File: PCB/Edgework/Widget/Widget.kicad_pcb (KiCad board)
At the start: 4 copper layers, 61 x 30 mm, 82 parts, among them J1 Edgework, J10 4, J11 SDA, J12 SCL, J13 1, J14 0, J15 5V, J16 3V3, J17 GND, J18 5V, J19 3V3, J2 ICSP, J20 GND, J21 5V, J22 3V3, J23 GND, J24 5V, J25 3V3, J26 GND, J3 11, J4 10, J5 9, J6 8, J7 7, J8 6, J9 5, Q1 Q_PMOS_GSD, Q2 Q_NMOS_GSD, Q3 Q_PMOS_GSD, Q4 Q_NMOS_GSD, Q5 Q_PMOS_GSD, Q6 Q_NMOS_GSD, Q7 Q_PMOS_GSD, Q8 Q_NMOS_GSD, U1 THVD1420DRLR, U2 PIC18F15Q40, U4 CM1293A‐04SO

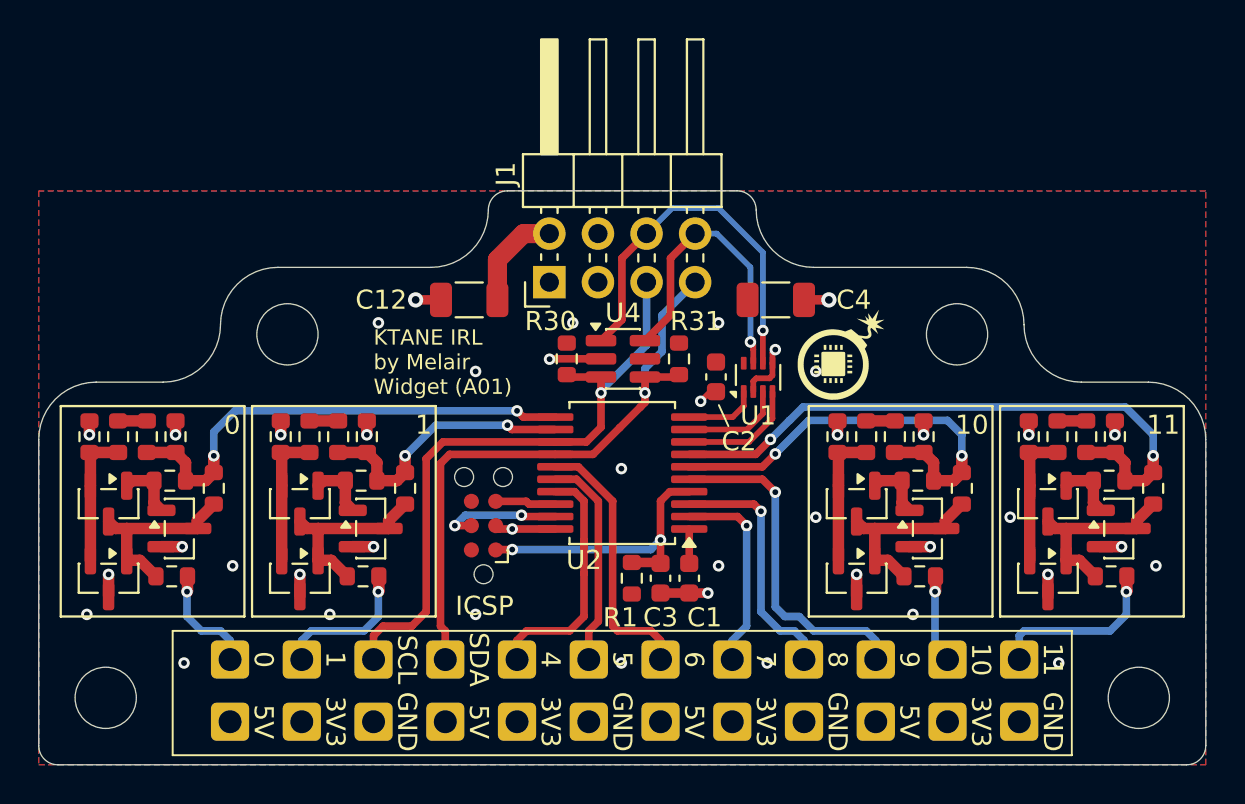
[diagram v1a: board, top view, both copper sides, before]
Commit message: feat: Migrate edgework to a STM32G070KBT6.
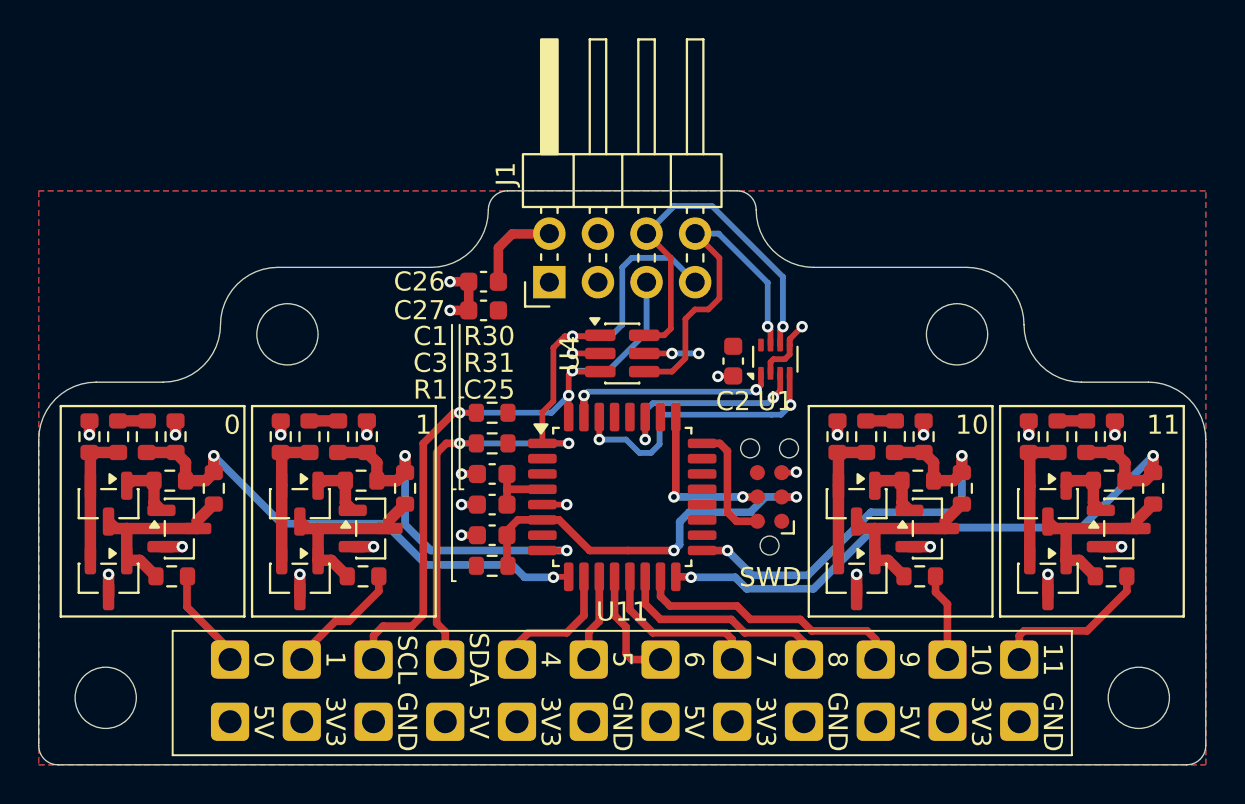
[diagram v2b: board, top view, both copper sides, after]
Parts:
- removed C12, C4: 100μF, Capacitor_SMD:C_1206_3216Metric
- removed U2: PIC18F15Q40, Package_SO:SSOP-20_5.3x7.2mm_P0.65mm
- added C25: 4.7uF, Capacitor_SMD:C_0603_1608Metric, F.Cu at (43.7, 39.8)
- added C26: 10uF, Capacitor_SMD:C_0603_1608Metric, F.Cu at (43.2, 29.8)
- added C27: 10uF, Capacitor_SMD:C_0603_1608Metric, F.Cu at (43.2, 31.2)
- added U11: STM32G070KBTx, Package_QFP:LQFP-32_7x7mm_P0.8mm, F.Cu at (50.5, 41.0)
- G***: moved to B.Cu
- H1, H2, H3, H4: footprint MountingHole:MountingHole_3.2mm_M3 -> KTANE:MountingHole_3.2mm_M3_NoCopper
- J2: value ICSP -> SWD
- R11, R18, R25, R4: value 100 -> 120
- moved J2 15.0 mm to (58.2, 41.0)
- moved C1 11.0 mm to (43.7, 41.4), turned to 180 degrees
- moved R31 10.7 mm to (43.7, 38.2), turned to 180 degrees
- moved C3 9.08 mm to (43.7, 43.0), turned to 180 degrees
- moved R1 7.33 mm to (43.7, 44.6), turned to 0 degrees
- moved R30 4.81 mm to (43.7, 36.6), turned to 180 degrees
- moved G*** 3.18 mm to (58.8, 33.2), turned to 180 degrees
- moved U1 1.31 mm to (58.5, 33.8)
- moved C2 1.22 mm to (56.3, 33.9)
- moved U4 0.28 mm to (50.5, 33.5)
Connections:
- C3 pad 1: ~{MCLR} -> ~{RESET}
- J2 pad 1: ~{MCLR} -> +3.3V
- J2 pad 2: +3.3V -> SWDIO
- J2 pad 3: GND -> ~{RESET}
- J2 pad 4: ICSPDAT -> SWCLK
- J2 pad 5: ICSPCLK -> GND
- R1 pad 2: ~{MCLR} -> ~{RESET}
- U4 pad 1: /A -> /SDA
- U4 pad 4: /SDA -> /B
- U4 pad 6: /B -> /A
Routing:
- net ~{RESET}: track 0.00 -> 20.7 mm, vias 0 -> 2
- net ~{MCLR}: track 15.3 -> 0.00 mm, vias 2 -> 0
- net BUS-TX: track 6.27 -> 15.0 mm, vias 0 -> 2
- net SWCLK: track 0.00 -> 8.58 mm, vias 0 -> 2
- net /GPIO6: track 14.1 -> 5.70 mm
- net BUS-RX: track 3.85 -> 11.2 mm, vias 0 -> 2
- net /GPIO5: track 11.4 -> 4.24 mm
- net /SDA: track 32.4 -> 38.8 mm, vias 1 -> 3
- net ICSPDAT: track 6.37 -> 0.00 mm, vias 2 -> 0
- net /GPIO4: track 12.8 -> 6.45 mm
- net SWDIO: track 0.00 -> 6.25 mm
- net BUS-DE: track 5.35 -> 11.1 mm, vias 0 -> 2
- net /IN_GPIO1: track 14.3 -> 19.6 mm
- net +3.3V: track 7.80 -> 12.2 mm, vias 0 -> 2
- net /GPIO9: track 17.8 -> 14.3 mm, vias 1 -> 0
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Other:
- board text added: "KTANE IRL by Melair Widget (B01)"
- board text removed: "KTANE IRL by Melair Widget (A01)"
